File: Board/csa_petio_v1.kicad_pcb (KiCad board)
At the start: 6 copper layers, 160 x 100 mm, 33 parts, among them IC12 7417N, IC16 74LVC8T245SO24, IC3 7400N, P1 C64KEYB, P2 IEEE488FLATCABLE, P3 PETUSERPORT, P4 CSABUS, P5 CBMTAPE, P6 CBMTAPE, P7 PETKEYBD, P8 PETKEYBDSUBD, U1 XC6SLX9-TQG144, U2 SN74LVC245APW, U3 SN74LVC245APW, U4 SN75160BDW, U5 SN75161BDW, U6 LSF0204Q, U7 LSF0204Q, U8 LSF0204Q, U9 LSF0204Q

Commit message: update
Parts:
- added UX16: AP2132BB, Package_SO:Diodes_PSOP-8, F.Cu at (115.8, 47.3)
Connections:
- IC16 pad 23: V12 -> V33
- IC16 pad 24: V12 -> V33
- R1 pad 1: V12 -> V33
- R2 pad 1: V12 -> V33
- U1 pad 103: unconnected-(U1A-VCCO_1-Pad103) -> V33
- U1 pad 122: unconnected-(U1A-VCCO_0-Pad122) -> V33
- U1 pad 125: unconnected-(U1A-VCCO_0-Pad125) -> V33
- U1 pad 129: V12 -> V33
- U1 pad 135: unconnected-(U1A-VCCO_0-Pad135) -> V33
- U1 pad 18: V12 -> V33
- U1 pad 20: V12 -> V33
- U1 pad 31: V12 -> V33
- U1 pad 36: V12 -> V33
- U1 pad 4: V12 -> V33
- U1 pad 42: V12 -> V33
- U1 pad 53: V12 -> V33
- U1 pad 63: V12 -> V33
- U1 pad 76: unconnected-(U1A-VCCO_1-Pad76) -> V33
- U1 pad 86: unconnected-(U1A-VCCO_1-Pad86) -> V33
- U1 pad 90: V12 -> V33
- U2 pad 1: V12 -> V33
- U2 pad 20: V12 -> V33
- U3 pad 1: V12 -> V33
- U3 pad 20: V12 -> V33
- UX17 pad 2: V12 -> V33
- UX18 pad 7: V12 -> V33
- UX18 pad 8: V12 -> V33

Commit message: adding keyboard, serial IEC
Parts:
- removed P8: PETKEYBDSUBD, csa_petio_v1:SUBD25F
- added C1: 100n, Capacitor_SMD:C_0805_2012Metric, F.Cu at (94.3, 44.1)
- added C2: 100n, Capacitor_SMD:C_0805_2012Metric, F.Cu at (114.5, 24.3)
- added C3: 100n, Capacitor_SMD:C_0805_2012Metric, F.Cu at (114.5, 27.3)
- added C4: 22u, Capacitor_SMD:C_0805_2012Metric_Pad1.18x1.45mm_HandSolder, F.Cu at (109.8, 24.3)
- added C5: 22u, Capacitor_SMD:C_0805_2012Metric_Pad1.18x1.45mm_HandSolder, F.Cu at (109.8, 27.3)
- added C6: 22u, Capacitor_SMD:C_0805_2012Metric_Pad1.18x1.45mm_HandSolder, F.Cu at (109.8, 30.3)
- added C7: 22u, Capacitor_SMD:C_0805_2012Metric_Pad1.18x1.45mm_HandSolder, F.Cu at (109.8, 33.3)
- added C8: 47u, Capacitor_SMD:C_0805_2012Metric_Pad1.18x1.45mm_HandSolder, F.Cu at (109.8, 36.3)
- added J1: DIN-6, csa_petio_v1:DIN6PIEC, F.Cu at (94.2, 34.4)
- added J14: Extended_PET_keyboard_connector, csa_petio_v1:PET_Extended_Keyboard_Connector, F.Cu at (65.8, -5.19)
- added J2: Conn_01x23, Connector_PinSocket_2.54mm:PinSocket_1x23_P2.54mm_Vertical, F.Cu at (50.3, -2.32)
- added JP18: JP1E, Connector_PinHeader_2.54mm:PinHeader_1x02_P2.54mm_Vertical, F.Cu at (1.79, 1.79)
- added JP22: JP1E, Connector_PinHeader_2.54mm:PinHeader_1x02_P2.54mm_Vertical, F.Cu at (6.38, 1.79)
- added R4: 330, Resistor_SMD:R_0603_1608Metric_Pad0.98x0.95mm_HandSolder, F.Cu at (114.4, 30.1)
- added R5: 10k, Resistor_SMD:R_0603_1608Metric_Pad0.98x0.95mm_HandSolder, F.Cu at (114.4, 32.6)
- added U10: 74LS06, Package_SO:SO-14_3.9x8.65mm_P1.27mm, F.Cu at (93.0, -2.24)
- added U11: SN74LVC245APW, Package_SO:TSSOP-20_4.4x6.5mm_P0.65mm, F.Cu at (87.7, 46.6)
- added U12: 4051, Package_SO:SOP-16_3.9x9.9mm_P1.27mm, F.Cu at (74.0, -1.60)
- added U13: 4051, Package_SO:SOP-16_3.9x9.9mm_P1.27mm, F.Cu at (82.5, -1.60)
- added U14: 74LVC1G04, Package_TO_SOT_SMD:SOT-23-5, F.Cu at (160.7, 47.7)
- R1: value 330 -> 4k7
- RN1: footprint csa_petio_v1:RN-9 -> Resistor_THT:R_Array_SIP9
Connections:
- IC16 pad 1: V12 -> V33
- IC16 pad 10: Net-(IC16-A8) -> D0
- IC16 pad 14: D7 -> Net-(IC16-B8)
- IC16 pad 15: D6 -> Net-(IC16-B7)
- IC16 pad 16: D5 -> Net-(IC16-B6)
- IC16 pad 17: D4 -> Net-(IC16-B5)
- IC16 pad 18: D3 -> Net-(IC16-B4)
- IC16 pad 19: D2 -> Net-(IC16-B3)
- IC16 pad 2: unconnected-(IC16-DIR-Pad2) -> R/-W
- IC16 pad 20: D1 -> Net-(IC16-B2)
- IC16 pad 21: D0 -> Net-(IC16-B1)
- IC16 pad 22: unconnected-(IC16-/OE-Pad22) -> /IOSEL
- IC16 pad 23: V33 -> V12
- IC16 pad 24: V33 -> V12
- IC16 pad 3: Net-(IC16-A1) -> D7
- IC16 pad 4: Net-(IC16-A2) -> D6
- IC16 pad 5: Net-(IC16-A3) -> D5
- IC16 pad 6: Net-(IC16-A4) -> D4
- IC16 pad 7: Net-(IC16-A5) -> D3
- IC16 pad 8: Net-(IC16-A6) -> D2
- IC16 pad 9: Net-(IC16-A7) -> D1
- P4 pad A15: Net-(IC16-A8) -> Net-(IC16-B1)
- P4 pad A16: Net-(IC16-A7) -> Net-(IC16-B2)
- P4 pad A17: Net-(IC16-A6) -> Net-(IC16-B3)
- P4 pad A18: Net-(IC16-A5) -> Net-(IC16-B4)
- P4 pad A19: Net-(IC16-A4) -> Net-(IC16-B5)
- P4 pad A20: Net-(IC16-A3) -> Net-(IC16-B6)
- P4 pad A21: Net-(IC16-A2) -> Net-(IC16-B7)
- P4 pad A22: Net-(IC16-A1) -> Net-(IC16-B8)
- P4 pad A24: unconnected-(P4-/IRQ-PadA24) -> Net-(P4-/IRQ)
- RN1 pad 1: unconnected-(RN1-Pad1) -> GND
- RN1 pad 2: /KI0 -> Net-(RN1-R1)
- RN1 pad 3: /KI1 -> Net-(RN1-R2)
- RN1 pad 4: /KI2 -> Net-(J2-Pin_1)
- RN1 pad 5: /KI3 -> Net-(J2-Pin_2)
- RN1 pad 6: /KI4 -> Net-(J2-Pin_3)
- RN1 pad 7: /KI5 -> Net-(J2-Pin_4)
- RN1 pad 8: /KI6 -> Net-(J2-Pin_5)
- RN1 pad 9: /KI7 -> Net-(J2-Pin_6)
- U1 pad 103: V33 -> GND
- U1 pad 114: unconnected-(U1A-IO_L65N_SCP2_0-Pad114) -> Net-(RN1-R1)
- U1 pad 115: unconnected-(U1A-IO_L65P_SCP3_0-Pad115) -> Net-(RN1-R2)
- U1 pad 116: unconnected-(U1A-IO_L64N_SCP4_0-Pad116) -> Net-(J2-Pin_1)
- U1 pad 117: unconnected-(U1A-IO_L64P_SCP5_0-Pad117) -> Net-(J2-Pin_2)
- U1 pad 118: unconnected-(U1A-IO_L63N_SCP6_0-Pad118) -> Net-(J2-Pin_3)
- U1 pad 119: unconnected-(U1A-IO_L63P_SCP7_0-Pad119) -> Net-(J2-Pin_4)
- U1 pad 120: unconnected-(U1A-IO_L62N_VREF_0-Pad120) -> Net-(J2-Pin_5)
- U1 pad 121: unconnected-(U1A-IO_L62P_0-Pad121) -> Net-(J2-Pin_6)
- U1 pad 122: V33 -> GND
- U1 pad 123: unconnected-(U1A-IO_L37N_GCLK12_0-Pad123) -> KSEL0
- U1 pad 124: unconnected-(U1A-IO_L37P_GCLK13_0-Pad124) -> KSEL1
- U1 pad 125: V33 -> GND
- U1 pad 126: unconnected-(U1A-IO_L36N_GCLK14_0-Pad126) -> KSEL2
- U1 pad 127: unconnected-(U1A-IO_L36P_GCLK15_0-Pad127) -> KSEL3
- U1 pad 131: unconnected-(U1A-IO_L35N_GCLK16_0-Pad131) -> Net-(U1A-IO_L35N_GCLK16_0)
- U1 pad 132: unconnected-(U1A-IO_L35P_GCLK17_0-Pad132) -> Net-(U1A-IO_L35P_GCLK17_0)
- U1 pad 133: unconnected-(U1A-IO_L34N_GCLK18_0-Pad133) -> Net-(U1A-IO_L34N_GCLK18_0)
- U1 pad 134: unconnected-(U1A-IO_L34P_GCLK19_0-Pad134) -> Net-(U1A-IO_L34P_GCLK19_0)
- U1 pad 135: V33 -> GND
- U1 pad 137: unconnected-(U1A-IO_L4N_0-Pad137) -> Net-(U11-B8)
- U1 pad 138: unconnected-(U1A-IO_L4P_0-Pad138) -> Net-(U11-B7)
- U1 pad 139: unconnected-(U1A-IO_L3N_0-Pad139) -> Net-(U11-B6)
- U1 pad 140: unconnected-(U1A-IO_L3P_0-Pad140) -> Net-(U11-B5)
- U1 pad 141: unconnected-(U1A-IO_L2N_0-Pad141) -> Net-(U11-B4)
- U1 pad 142: unconnected-(U1A-IO_L2P_0-Pad142) -> Net-(U11-B3)
- U1 pad 143: unconnected-(U1A-IO_L1N_VREF_0-Pad143) -> Net-(U11-B2)
- U1 pad 144: unconnected-(U1A-IO_L1P_HSWAPEN_0-Pad144) -> Net-(U11-B1)
- U1 pad 71: unconnected-(U1C-DONE_2-Pad71) -> Net-(U1C-DONE_2)
- U1 pad 76: V33 -> GND
- U1 pad 86: V33 -> GND

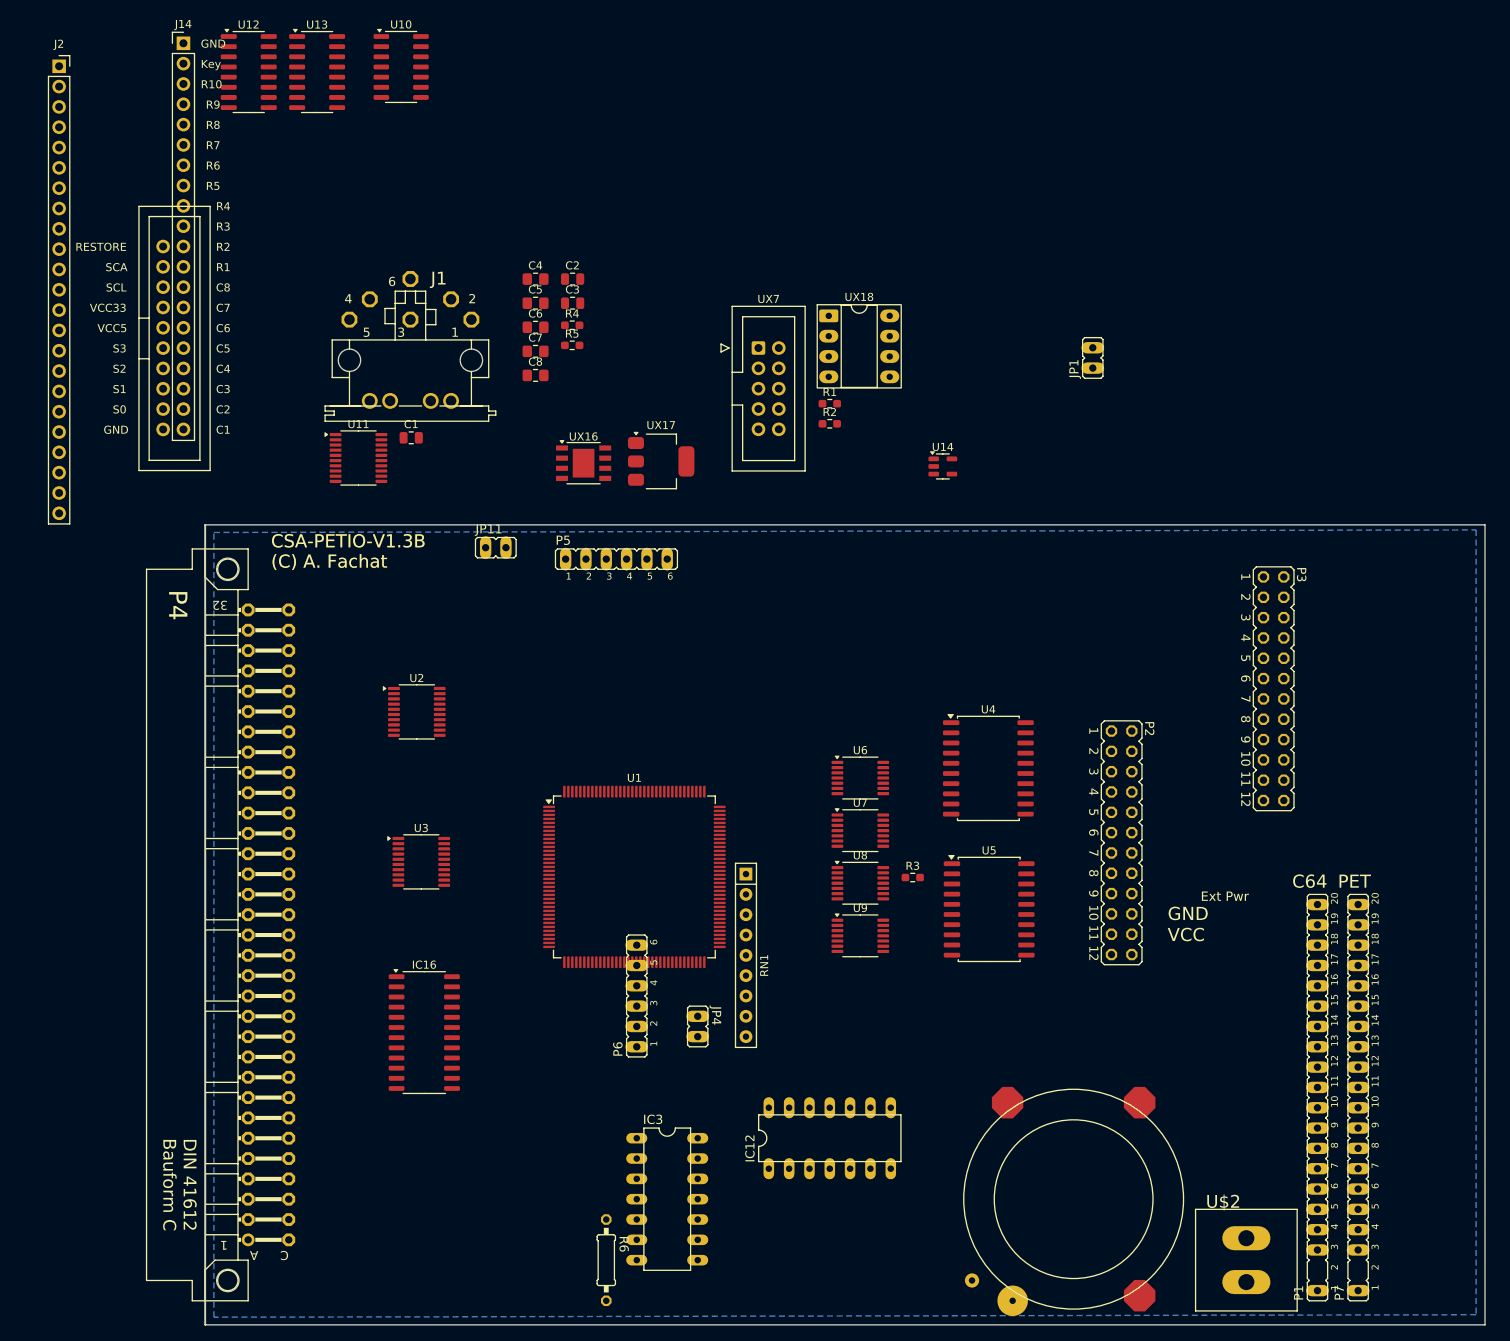
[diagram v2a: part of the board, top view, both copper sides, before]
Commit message: add serial, SPI-10-5V
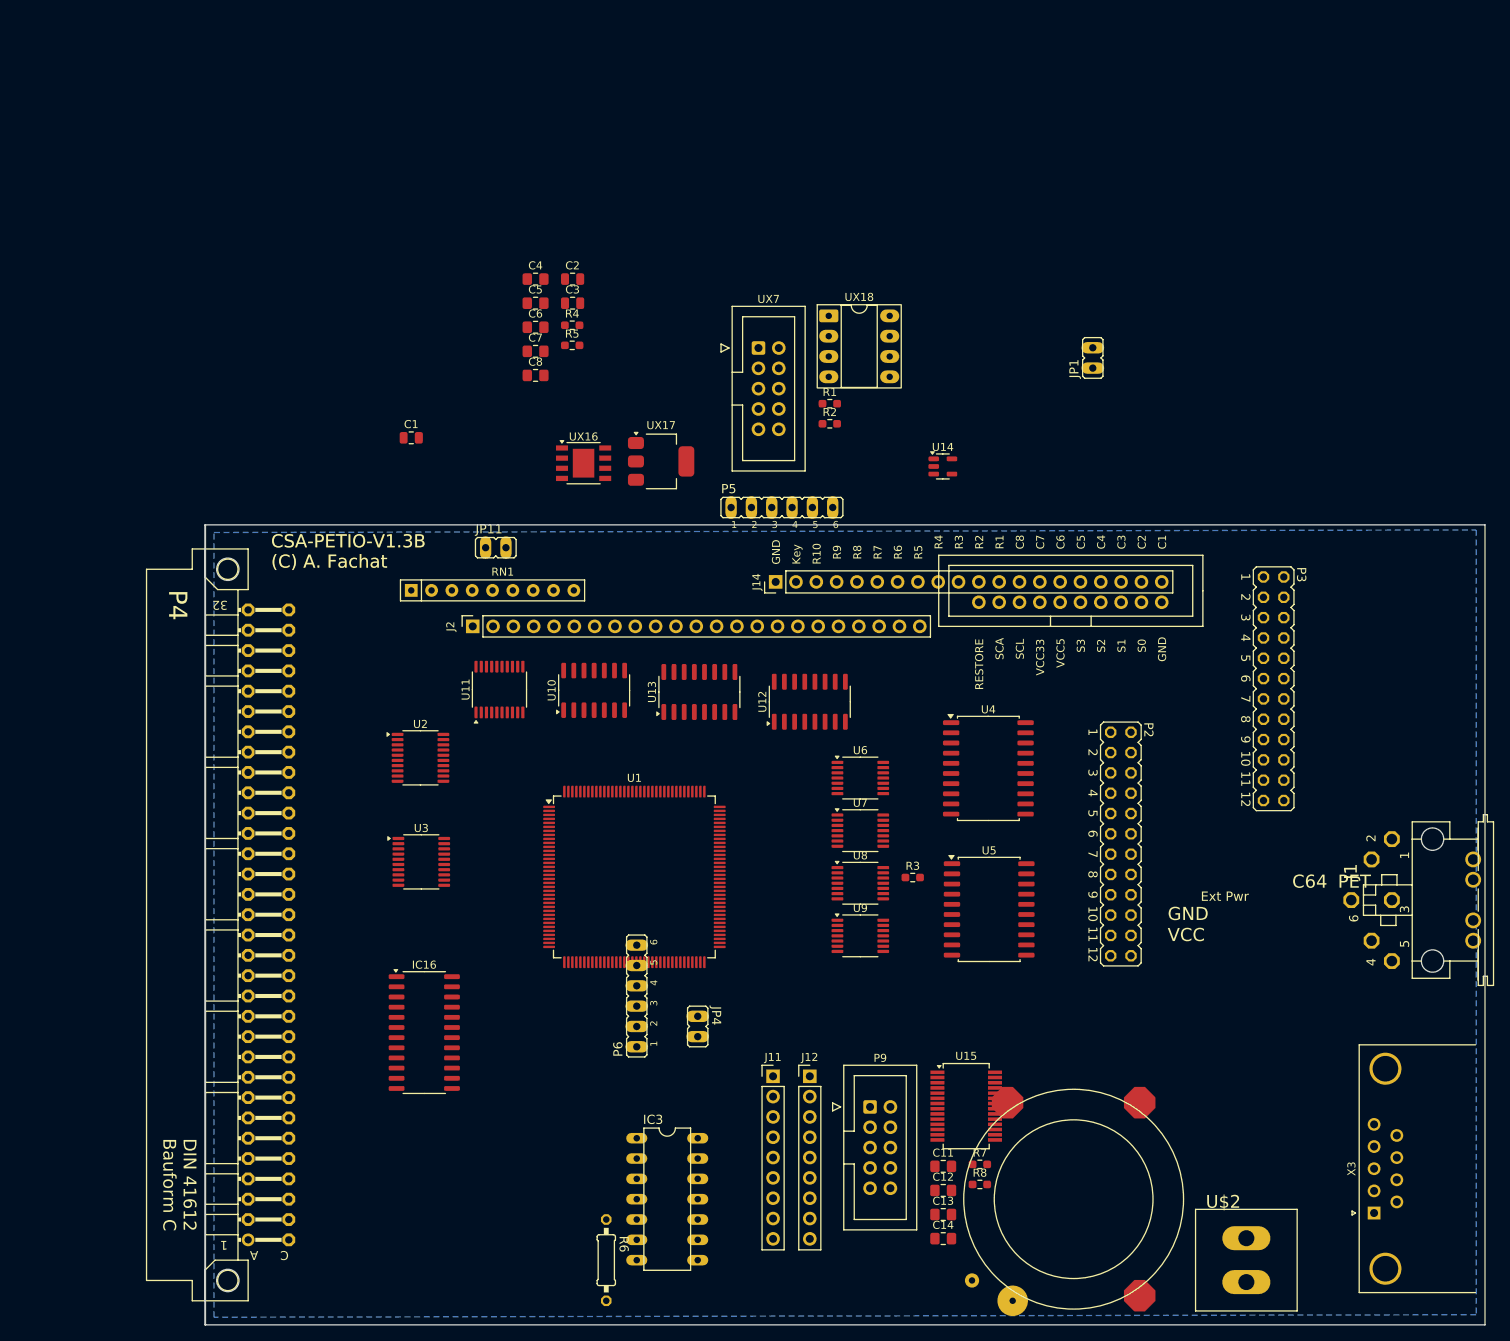
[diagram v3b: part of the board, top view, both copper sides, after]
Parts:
- removed IC12: 7417N, csa_petio_v1:DIL14
- removed P1: C64KEYB, csa_petio_v1:C64KEYB
- removed P7: PETKEYBD, csa_petio_v1:C64KEYB
- added C11: 1u, Capacitor_SMD:C_0805_2012Metric_Pad1.18x1.45mm_HandSolder, F.Cu at (160.8, 135.2)
- added C12: 1u, Capacitor_SMD:C_0805_2012Metric_Pad1.18x1.45mm_HandSolder, F.Cu at (160.8, 138.2)
- added C13: 1u, Capacitor_SMD:C_0805_2012Metric_Pad1.18x1.45mm_HandSolder, F.Cu at (160.8, 141.2)
- added C14: 1u, Capacitor_SMD:C_0805_2012Metric_Pad1.18x1.45mm_HandSolder, F.Cu at (160.8, 144.2)
- added J11: Conn_01x09, Connector_PinHeader_2.54mm:PinHeader_1x09_P2.54mm_Vertical, F.Cu at (139.5, 123.9)
- added J12: Conn_01x09, Connector_PinHeader_2.54mm:PinHeader_1x09_P2.54mm_Vertical, F.Cu at (144.1, 123.9)
- added P9: ~, Connector_IDC:IDC-Header_2x05_P2.54mm_Vertical, F.Cu at (151.6, 127.8)
- added R7: 330, Resistor_SMD:R_0603_1608Metric_Pad0.98x0.95mm_HandSolder, F.Cu at (165.4, 134.9)
- added R8: 330, Resistor_SMD:R_0603_1608Metric_Pad0.98x0.95mm_HandSolder, F.Cu at (165.4, 137.5)
- added U15: ADM560, Package_SO:SSOP-28_5.3x10.2mm_P0.65mm, F.Cu at (163.7, 127.7)
- added X3: M09HPS, Connector_Dsub:DSUB-9_Pins_Horizontal_P2.77x2.84mm_EdgePinOffset9.90mm_Housed_MountingHolesOffset11.32mm, F.Cu at (214.6, 141.0)
- moved J1 144.5 mm to (221.9, 101.9), turned to 90 degrees
- moved U12 105.4 mm to (144.1, 77.1), turned to 90 degrees
- moved J14 100.1 mm to (139.8, 62.1), turned to 90 degrees
- moved U13 91.0 mm to (130.3, 75.9), turned to 90 degrees
- moved J2 87.0 mm to (102.0, 67.7), turned to 90 degrees
- moved U10 81.6 mm to (117.1, 75.7), turned to 90 degrees
- moved RN1 54.8 mm to (94.3, 63.2), turned to 0 degrees
- moved U11 33.9 mm to (105.3, 75.6), turned to 90 degrees
- moved P5 21.7 mm to (141.9, 54.1)
- moved U2 5.76 mm to (95.4, 84.1)
- moved P2 0.18 mm to (183.0, 94.9)
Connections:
- net Net-(P4-/IRQ) renamed /BIRQ
- net Net-(P4-/RES) renamed /BRES
- net Net-(U11-A1) renamed /IO2/SATN
- net Net-(U11-A2) renamed /IO2/DATA
- net Net-(U11-A3) renamed /IO2/SLOWCLK
- net Net-(U11-A4) renamed /IO2/FASTCLK
- net Net-(U1A-IO_L34P_GCLK19_0) renamed CLKOUT
- JP4 pad 2: Net-(IC12E-O) -> unconnected-(JP4-Pad2)
- U1 pad 18: V33 -> V12
- U1 pad 31: V33 -> V12
- U1 pad 39: unconnected-(U1B-IO_L65P_INIT_B_2-Pad39) -> /IO1/LDCD
- U1 pad 4: V33 -> V12
- U1 pad 40: unconnected-(U1B-IO_L64N_D9_2-Pad40) -> /IO1/LCTS
- U1 pad 41: unconnected-(U1B-IO_L64P_D8_2-Pad41) -> /IO1/LDSR
- U1 pad 42: V33 -> V12
- U1 pad 43: unconnected-(U1B-IO_L62N_D6_2-Pad43) -> /IO1/LRI
- U1 pad 44: unconnected-(U1B-IO_L62P_D5_2-Pad44) -> /IO1/LRX
- U1 pad 45: unconnected-(U1B-IO_L49N_D4_2-Pad45) -> /IO1/LTX
- U1 pad 46: unconnected-(U1B-IO_L49P_D3_2-Pad46) -> /IO1/LDTR
- U1 pad 47: unconnected-(U1B-IO_L48N_RDWR_B_VREF_2-Pad47) -> /IO1/LRTS
- U1 pad 48: unconnected-(U1B-IO_L48P_D7_2-Pad48) -> RCTS
- U1 pad 50: unconnected-(U1B-IO_L31N_GCLK30_D15_2-Pad50) -> RTX
- U1 pad 51: unconnected-(U1B-IO_L31P_GCLK31_D14_2-Pad51) -> RRX
- U1 pad 55: unconnected-(U1B-IO_L30N_GCLK0_USERCCLK_2-Pad55) -> /IO1/RRTS
- U1 pad 56: unconnected-(U1B-IO_L30P_GCLK1_D13_2-Pad56) -> /IO1/RDSR
- U1 pad 57: unconnected-(U1B-IO_L14N_D12_2-Pad57) -> /IO1/RDTR
- U1 pad 63: V33 -> V12
- U1 pad 66: unconnected-(U1B-IO_L2N_CMPMOSI_2-Pad66) -> Net-(P9-/SEL)
- U1 pad 67: unconnected-(U1B-IO_L2P_CMPCLK_2-Pad67) -> Net-(U1B-IO_L2P_CMPCLK_2)
